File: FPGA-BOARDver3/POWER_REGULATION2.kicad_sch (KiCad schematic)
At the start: 75 parts, among them J7 Conn_01x06_Pin, Q8 FDV301N, U19 NL17SZ17XV5T2G, U20 FPF1018, U21 NC7WZ07P6X, U22 TPS65400RGZT, U9 SIP32510DT-T1-GE3

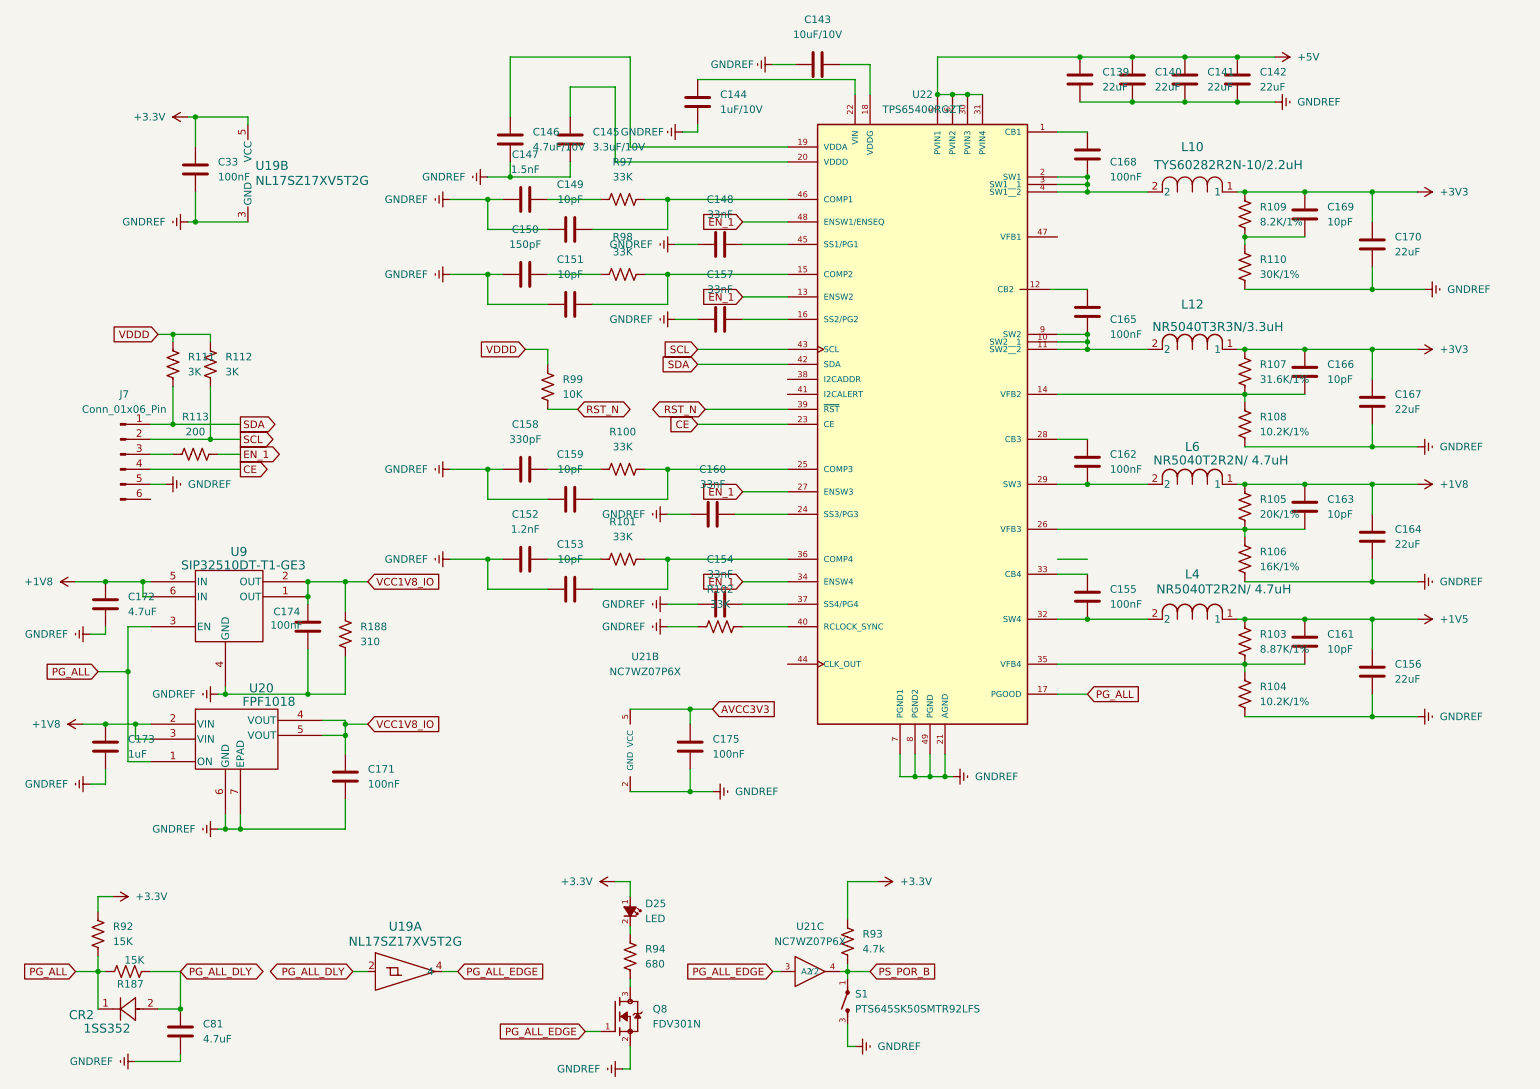
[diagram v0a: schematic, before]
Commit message: added audio out and usb
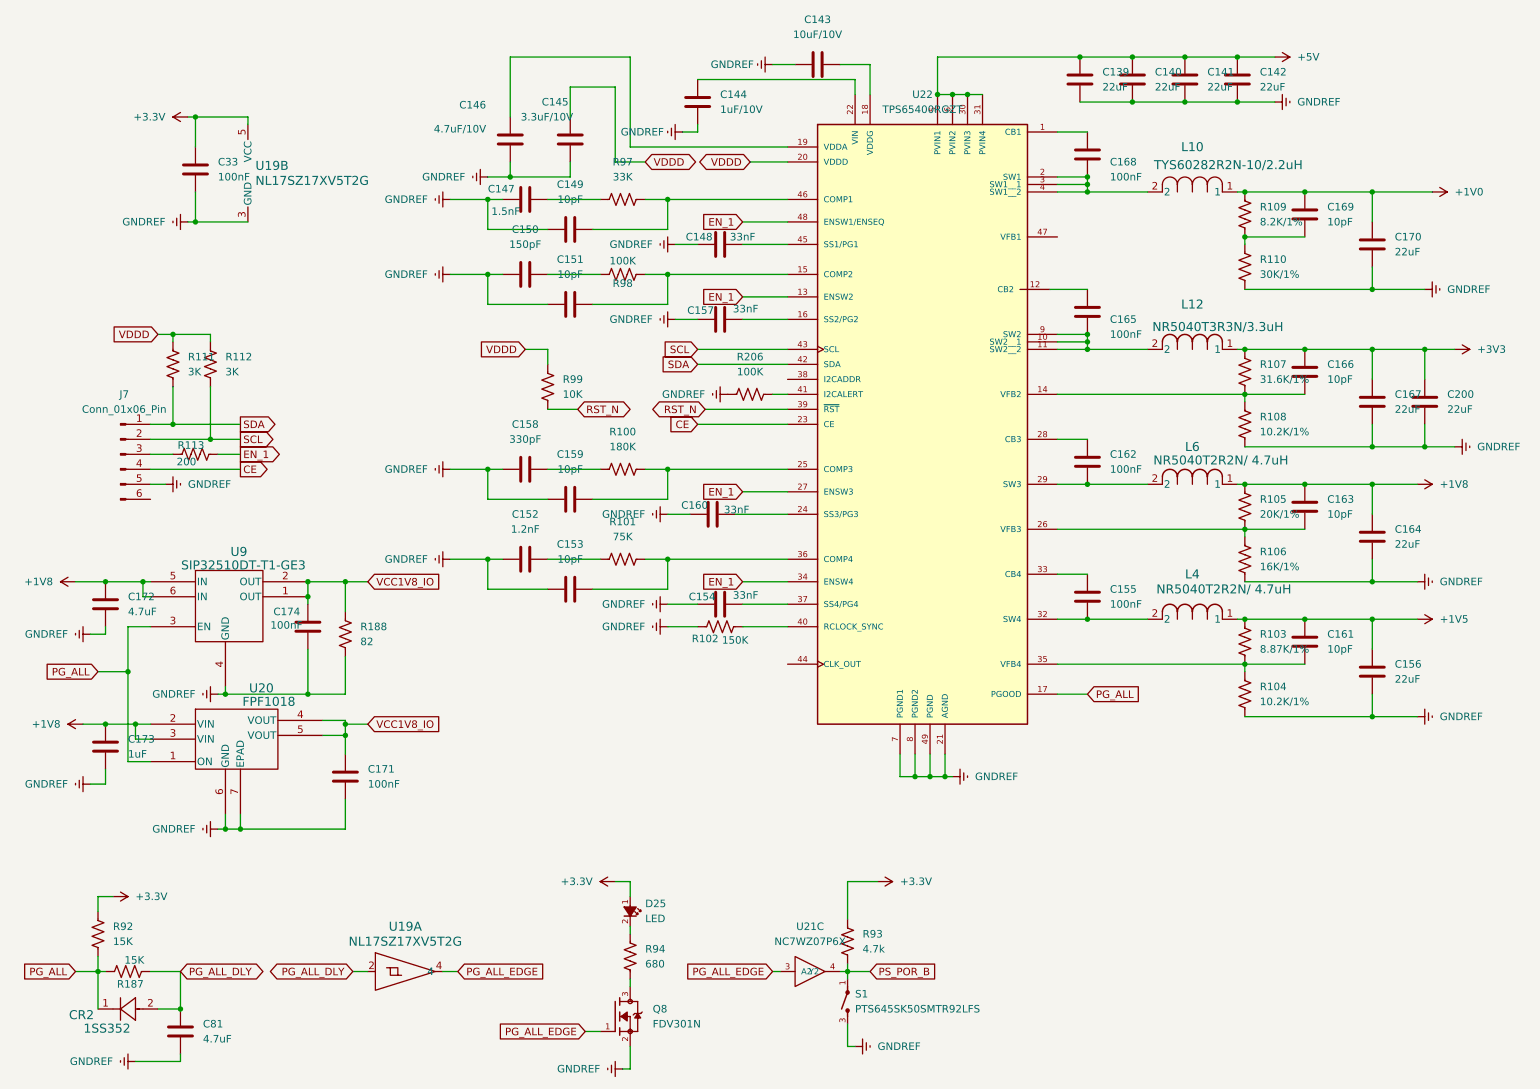
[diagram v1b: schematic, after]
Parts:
- removed C175: 100nF, footprints:C_0402, symbol Device:C
- removed unit 2 of U21
- added C200: 22uF, footprints:C_0402, symbol Device:C
- added R206: 100K, footprints:R_0402, symbol Device:R_US
- R100: value 33K -> 180K
- R101: value 33K -> 75K
- R102: value 33K -> 150K
- R188: value 310 -> 82
- R98: value 33K -> 100K
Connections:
- net +3V3: now also C200.1; no longer C169.1, C170.1, L10.1, R109.1
- net GNDREF: now also C200.2, R206.1
- net VDDD: now also C145.1, U22.20 (VDDD)
- net at U22.41 (I2CALERT): now also R206.2
- new net +1V0: C169.1, C170.1, L10.1, R109.1

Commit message: updated schematic and layout
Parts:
- removed J7: Conn_01x06_Pin, footprints:CONN6_PZ254V-11-06P_XFC, symbol Connector:Conn_01x06_Pin
- removed L12: NR5040T3R3N/3.3uH, footprints:IND_TAIYO_NR5040_TAY, symbol 2025-03-18_07-07-44:NR5040T3R3N
- removed L4: NR5040T2R2N/ 4.7uH, footprints:IND_TAIYO_NR5040_TAY, symbol 2025-03-04_21-33-04:NR5040T2R2N
- removed R111, R112: 3K, footprints:R_0402, symbol Device:R_US
- removed R113: 200, footprints:R_0402, symbol Device:R_US
- added L5: SRP6540-1R5M, footprints:IND_SRP6540-1R5M, symbol SRP4020TA_1R5M:SRP4020TA-1R5M
- added L7: NR5040T4R7N/ 4.7uH, footprints:IND_TAIYO_NR5040_TAY, symbol 2025-03-04_21-33-04:NR5040T2R2N
- C139, C140, C141, C142, C156, C164, C167, C170, C200: LCSC PN (none) -> c415703
- C143: LCSC PN (none) -> c315248
- C144, C173: LCSC PN (none) -> c14445
- C145: LCSC PN (none) -> c51412
- C146, C172, C81: LCSC PN (none) -> c23733
- C147: LCSC PN (none) -> c23967
- C148, C154, C157, C160: LCSC PN (none) -> c472437
- C149, C151, C153, C159, C161, C163, C166, C169: LCSC PN (none) -> c307440
- C150: LCSC PN (none) -> c1527
- C152: LCSC PN (none) -> c393671
- C155, C162, C165, C168, C171, C174, C33: LCSC PN (none) -> c1525
- C158: LCSC PN (none) -> c13533
- CR2: LCSC PN (none) -> C15885
- D25: LCSC PN (none) -> C434449
- L6: value NR5040T2R2N/ 4.7uH -> NR5040T4R7N/ 4.7uH; LCSC PN (none) -> C223063
- Q8: LCSC PN (none) -> C15310
- R100: LCSC PN (none) -> C138046
- R101: LCSC PN (none) -> C137935
- R102: LCSC PN (none) -> C93947
- R103: LCSC PN (none) -> C48391747
- R104, R108: LCSC PN (none) -> C138069
- R105: LCSC PN (none) -> C93942
- R106: LCSC PN (none) -> C163487
- R107: LCSC PN (none) -> C276265
- R109: LCSC PN (none) -> C137929
- R110: LCSC PN (none) -> C138008
- R187, R92: LCSC PN (none) -> C114761
- R188: LCSC PN (none) -> C163453
- R206: value 100K -> 10K; LCSC PN (none) -> C60490
- R93: LCSC PN (none) -> C105871
- R94: LCSC PN (none) -> C137948
- R97: LCSC PN (none) -> C138003
- R98: LCSC PN (none) -> C60491
- R99: LCSC PN (none) -> C60490
- S1: LCSC PN (none) -> C221872
- U19: LCSC PN (none) -> C152502
- U21: LCSC PN (none) -> C95342
- U22: LCSC PN (none) -> C201658
- U9: LCSC PN (none) -> C145264
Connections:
- net +3.3V is gone; now on net +3V3: C33.1, D25.1 (A), R92.1, R93.1, U19.5 (VCC)
- net +1V5: now also L7.1
- net +3V3: now also L5.1
- net +5V: now also C144.1, U22.22 (VIN)
- net at C165.2, U22.10 (SW2__1), U22.11 (SW2__2)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: now also L5.2
- net at C155.2, U22.32 (SW4): now also L7.2
- net at U22.47 (VFB1): now also C169.2, R109.2, R110.1
